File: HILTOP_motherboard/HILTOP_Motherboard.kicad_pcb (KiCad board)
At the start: 6 copper layers, 170 x 170 mm, 758 parts, among them J1 BACKPLANE_PWR, J10 HDMI, J11 DISP_PWR, J12 DISPLAY_PORT, J13 DDR2_SODIMM_COMPUTE_MODULE_3, J14 VADJ_B, J15 VADJ_A, J16 SOFT_START_PWR, J17 PWR_LED, J18 USB_B, J19 Micro_SD_Card, J2 ATX_MOLEX_02X12, J20 CAMERA_PORT, J21 EXT_FAN, J22 BACKPLANE_LV_PWR, J23 EXT_FAN, J24 HILTOP_PCIE-64_CONN, J25 DEBUG, J26 IO_EXP, J3 SATA, J4 USB_A_DOUBLE, J5 USB FRONT PANEL, J6 CAN, J7 RS485, J8 EXT_TEMP_MON, J9 RJ45-TRANS_SI-61001-F, Q1 Si7148DP-T1-E3, Q2 Si7148DP-T1-E3, Q3 2N7002, Q4 2N7002, Q5 ZXMN6A07F, Q6 ZXMN6A07F, Q7 ZXMN6A07F, Q8 SSM3J328R, U1 LM337BD2TG, U10 TLC271, U11 ADS1015, U12 MCP4725, U13 CME0505S3C, U14 SP3003-02XJ, U15 ISO3080, U16 ISO3080, U17 CME0505S3C, U18 USB6B1, U19 USB6B1, U2 MIC2026-1YM, U20 USB6B1, U21 USB6B1, U22 BQ32000, U23 TPD12S016, U24 MAX16054, U25 STM6719SFWB6F, U26 LM75B, U27 TPS54394, U28 LP2985, U29 CME0505S3C, U3 USB2517, U30 MCP2517FD, U31 MCP2517FD, U32 CME0505S3C, U33 ADuM1201, U34 ADuM1201, U35 MCP2561FD, U36 MCP2561FD, U37 TUSB9261, U38 AT25DN512CSSHF-B, U39 MCP23017, U4 MIC2026-1YM, U40 SP3003-02XJ, U41 CP2102N-A01-GQFN24, U43 MAX3107, U44 MAX3107, U45 93AAxxA, U5 SP3003-02XJ, U6 SP3003-02XJ, U7 LAN7500, U8 LM5118, U9 INA250A3, Y1 24MHz Crystal, Y2 25MHz Crystal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

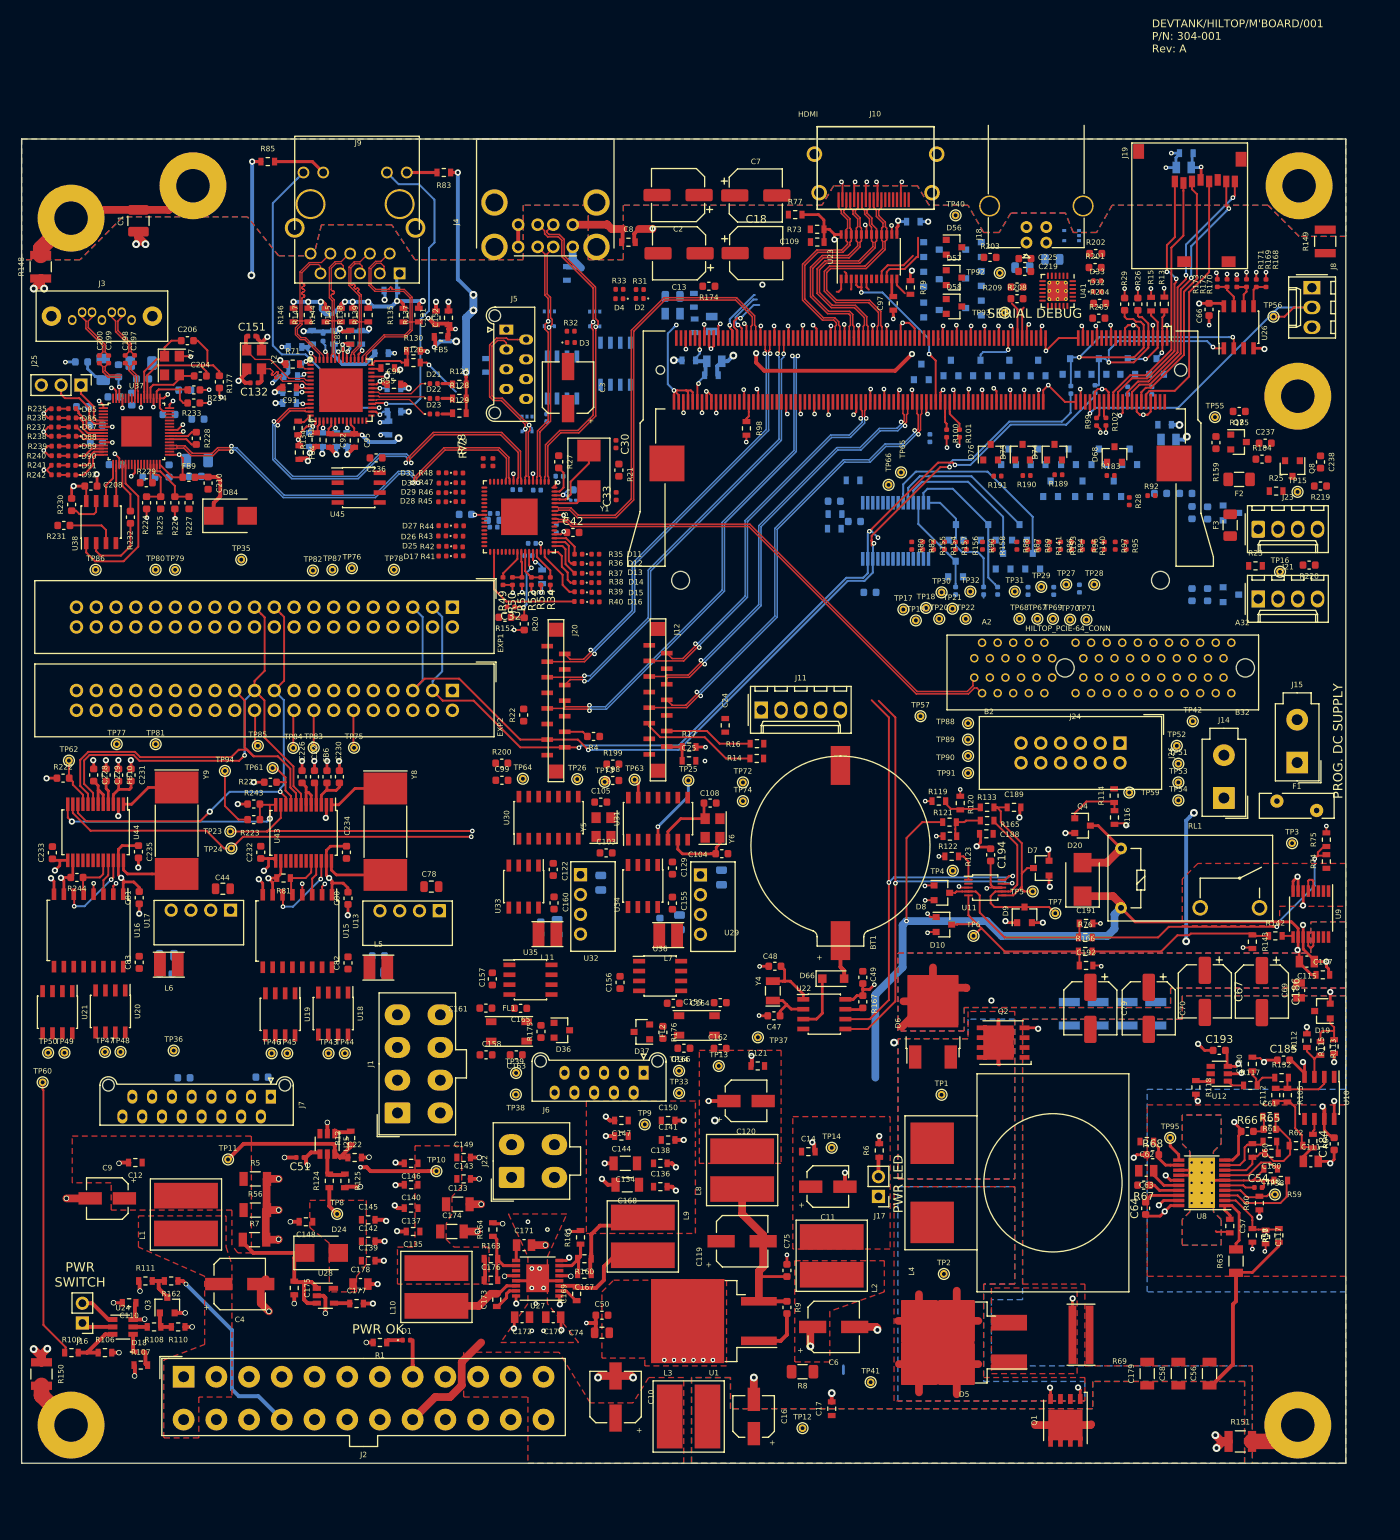
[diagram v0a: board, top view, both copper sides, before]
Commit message: 90% complete on backplane and IO connectors
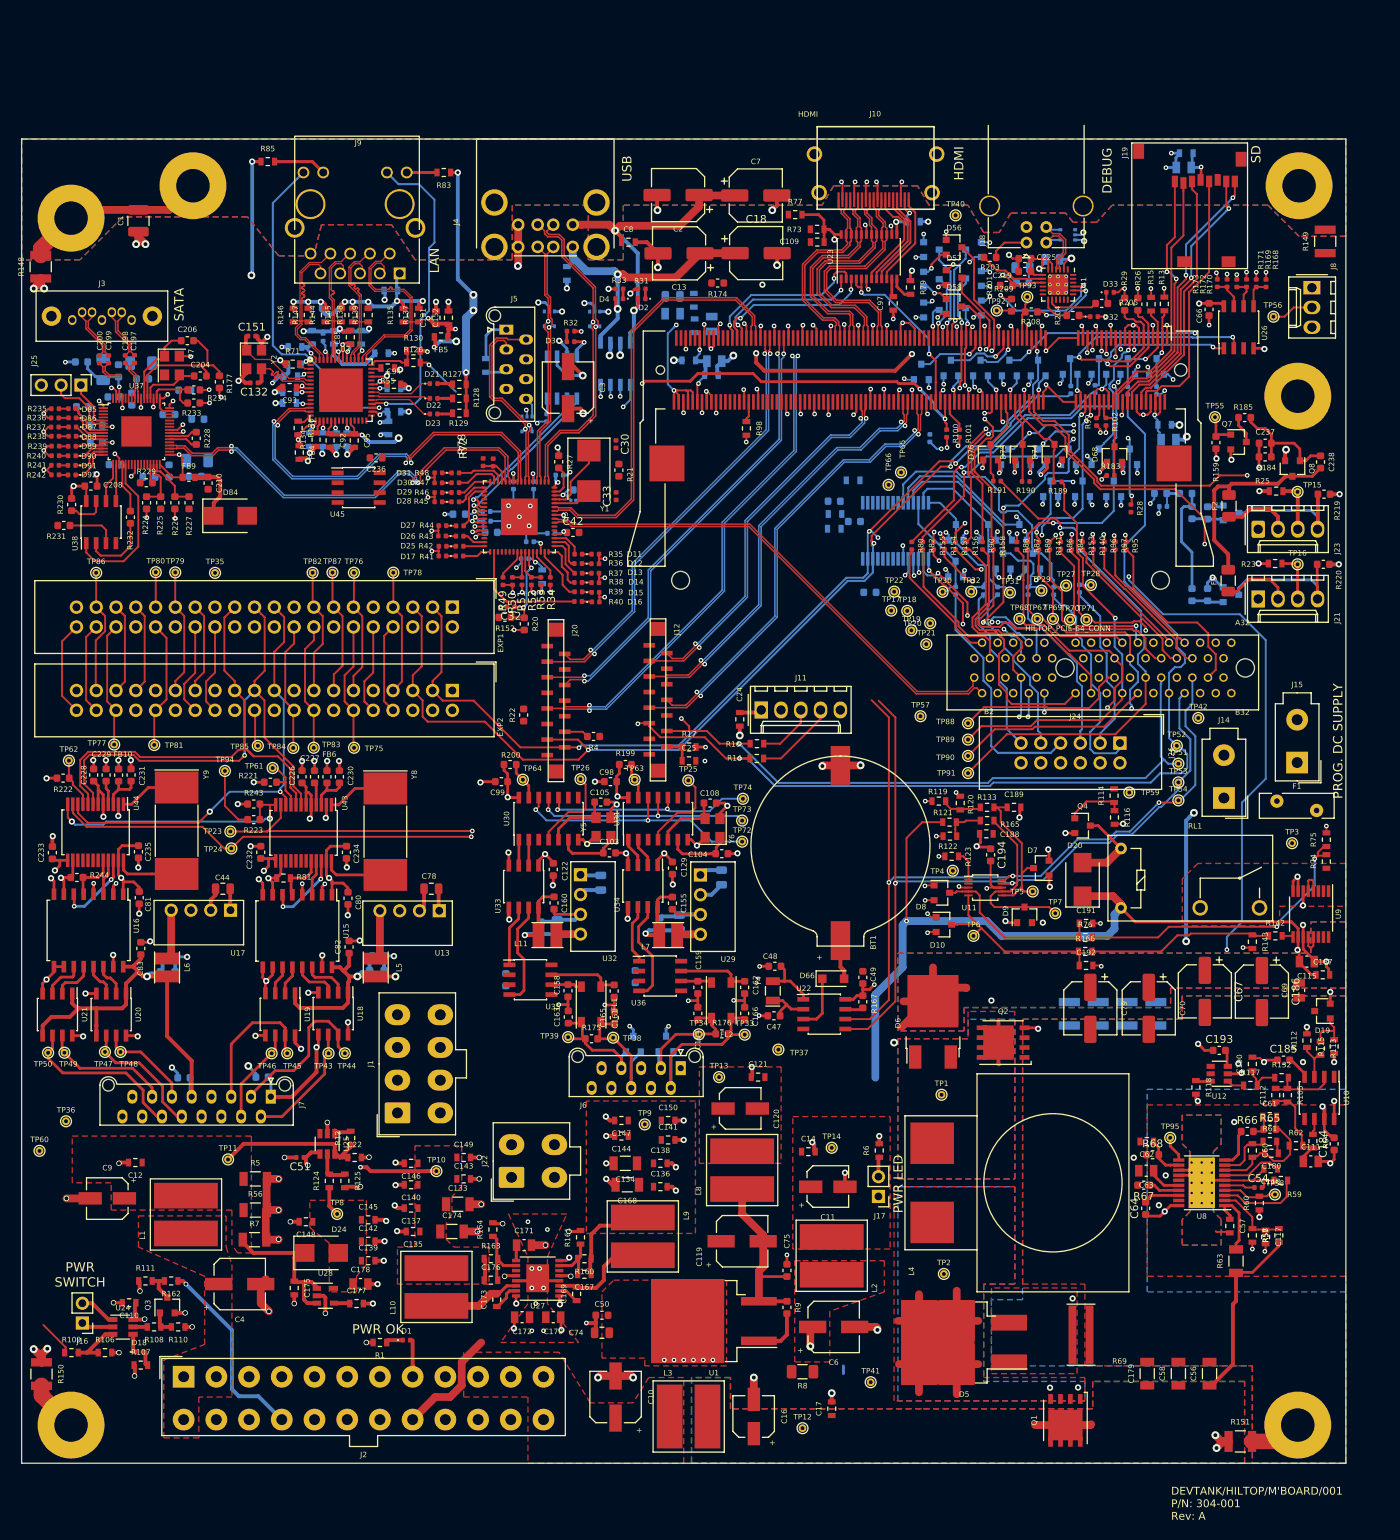
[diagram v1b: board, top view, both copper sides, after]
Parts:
- C156, C157, D36, D37, R202, R92: moved to B.Cu
- moved TP73 18.3 mm to (142.5, 137.5)
- moved C161 16.6 mm to (126.1, 159.4), turned to 270 degrees
- moved TP36 16.5 mm to (55.7, 176.1)
- moved TP38 14.5 mm to (125.9, 165.4)
- moved C158 13.4 mm to (120.1, 159.3), turned to 270 degrees
- moved C165 12.1 mm to (126.1, 162.8), turned to 90 degrees
- moved R201 11.6 mm to (176.4, 68.8), turned to 180 degrees
- moved TP33 11.3 mm to (142.8, 165.0)
- moved FL1 11.1 mm to (123.1, 161.1), turned to 270 degrees
- moved R202 10.1 mm to (178.5, 68.5)
- moved TP22 9.82 mm to (162.0, 108.1)
- moved D36 9.35 mm to (128.5, 166.2), turned to 90 degrees
- moved C166 8.99 mm to (142.8, 162.2), turned to 90 degrees
- moved TP60 8.81 mm to (52.3, 179.9)
- moved C162 8.44 mm to (142.8, 158.9), turned to 270 degrees
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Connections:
- J13 pad 46: /FAN_SENSE_2 -> /FAN_SENSE_1
- J13 pad 48: /FAN_SENSE_1 -> /FAN_SENSE_2
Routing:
- net /I2C0_SDA: track 11.4 -> 202.3 mm, vias 0 -> 3
- net /I2C0_SCL: track 15.0 -> 201.5 mm, vias 0 -> 2
- net /SYS_PWM1: track 0.00 -> 184.8 mm, vias 0 -> 2
- net /ATX_PWR_SHDN: track 39.3 -> 209.7 mm, vias 0 -> 3
- net /PWR_SW: track 4.76 -> 174.4 mm
- net GND: track 421.3 -> 588.5 mm, vias 224 -> 297
- net /SPI0_SCLK: track 49.6 -> 212.2 mm, vias 0 -> 1
- net /SPI0_CS1: track 0.00 -> 161.6 mm, vias 0 -> 1
- net /SYS_PWM0: track 0.07 -> 157.1 mm, vias 0 -> 1
- net /SYS_TRIG: track 0.00 -> 148.1 mm
- net /SPI0_MOSI: track 56.5 -> 199.8 mm, vias 2 -> 3
- net /SPI1_MOSI: track 0.00 -> 142.0 mm, vias 0 -> 2
- net /PR_GPIO22: track 0.00 -> 141.9 mm, vias 0 -> 2
- net /SPI1_MISO: track 0.00 -> 139.5 mm, vias 0 -> 2
- net /DC_DC_ENABLE: track 6.98 -> 136.9 mm, vias 0 -> 3
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- added copper zone on In3.Cu, net +1V8
- added copper zone on In3.Cu, net +5V
- added copper zone on In3.Cu, net Earth
- added copper zone on In3.Cu, net GND
- added copper zone on In1.Cu, net GND_ISO3
- added copper zone on In1.Cu, net GND_ISO4
- added copper zone on In3.Cu, net Net-(C6-Pad1)
- removed copper zone on In2.Cu, net +1V8
- removed copper zone on In2.Cu, net +5V
- removed copper zone on In2.Cu, net Earth
- removed copper zone on In2.Cu, net GND
- removed copper zone on In2.Cu, net Net-(C6-Pad1)
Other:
- board text added: "DEBUG"
- board text added: "HDMI"
- board text added: "LAN"
- board text added: "LAYER STACK UP: Layer 1 - Signal - F.Cu Layer 2 - Ground - In1.Cu Layer 3 - Signal - In2.Cu Layer 4 - Power - In3.Cu Layer 5 - Ground - In4.Cu Layer 6 - Signal - B.Cu"
- board text added: "SATA"
- board text added: "SD"
- board text added: "USB"
- board text removed: "SERIAL DEBUG"

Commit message: nearly all tracked - power and ground planes to do!
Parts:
- C77: moved to F.Cu
- R174: moved to B.Cu
- moved R174 12.4 mm to (131.2, 77.9), turned to 0 degrees
- moved TP17 7.28 mm to (168.4, 113.2)
- moved C68 6.36 mm to (131.0, 76.0)
- moved TP21 5.87 mm to (162.2, 110.5)
- moved TP57 5.75 mm to (166.7, 118.5)
- moved TP88 4.80 mm to (167.6, 127.8)
- moved C77 4.22 mm to (160.7, 104.4)
- moved R10 4.16 mm to (154.3, 102.3)
- moved TP18 3.33 mm to (166.8, 111.8)
- moved TP20 3.24 mm to (164.3, 110.0)
- moved R103 2.52 mm to (133.8, 70.5), turned to 0 degrees
- moved TP59 2.30 mm to (193.6, 135.7)
- moved TP90 2.22 mm to (169.3, 129.3)
- moved R114 1.94 mm to (190.9, 136.1), turned to 0 degrees
- moved C236 1.70 mm to (97.0, 90.1), turned to 90 degrees
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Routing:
- net +5V: track 196.6 -> 704.7 mm, vias 17 -> 24
- net /~MASTER_RESET: track 17.4 -> 329.6 mm, vias 1 -> 6
- net +2V5: track 90.8 -> 385.4 mm, vias 13 -> 14
- net +12V: track 141.5 -> 344.7 mm, vias 4 -> 6
- net /UART_CH2_CS: track 6.35 -> 172.7 mm, vias 0 -> 1
- net +1V8: track 12.7 -> 168.8 mm, vias 0 -> 3
- net /SPI1_CS2_CAM_IO1: track 40.1 -> 193.7 mm, vias 0 -> 1
- net /UART_CH1_CS: track 9.37 -> 144.2 mm, vias 1 -> 3
- net /PR_GPIO26: track 46.4 -> 178.4 mm, vias 0 -> 1
- net /SPI0_CS0: track 21.0 -> 150.4 mm, vias 1 -> 2
- net /PR_GPIO25: track 29.9 -> 156.0 mm, vias 1 -> 2
- net /SPI0_MISO: track 87.0 -> 210.1 mm, vias 1 -> 2
- net /SPI1_CS0: track 32.3 -> 152.5 mm
- net /SPI1_CS1_CAM_IO0: track 35.3 -> 155.1 mm, vias 0 -> 1
- net /SYS_CLK0: track 16.1 -> 122.7 mm, vias 0 -> 4
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- added copper zone on In4.Cu, net Earth
- added copper zone on In1.Cu, net GND_ISO1
- added copper zone on In1.Cu, net GND_ISO2
- removed copper zone on In3.Cu, net Earth
